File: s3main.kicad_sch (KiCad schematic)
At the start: 137 parts, among them J1 TRACK, J2 IDC, J3 POWER, J4 USB_C_Receptacle_USB2.0_16P, J5 ZUSI, Q1 QS6K21, Q10 BC847B, Q11 BC847B, Q2 BC847BDW1, Q3 SiS4634LDN, Q4 SiS4634LDN, Q5 SiS4634LDN, Q6 QS6K21, Q7 SiS4634LDN, Q8 SiS4634LDN, Q9 BC857B, SW1 EN, SW2 BOOT, U1 LM393, U10 BTS4141N, U2 7402, U3 TLV9061xDBV, U4 ESP32-S3-WROOM-2, U5 DRV8328B, U6 TPS281C100A, U7 AP63205WU, U8 TXS0102DCT, U9 AZ1117-3.3

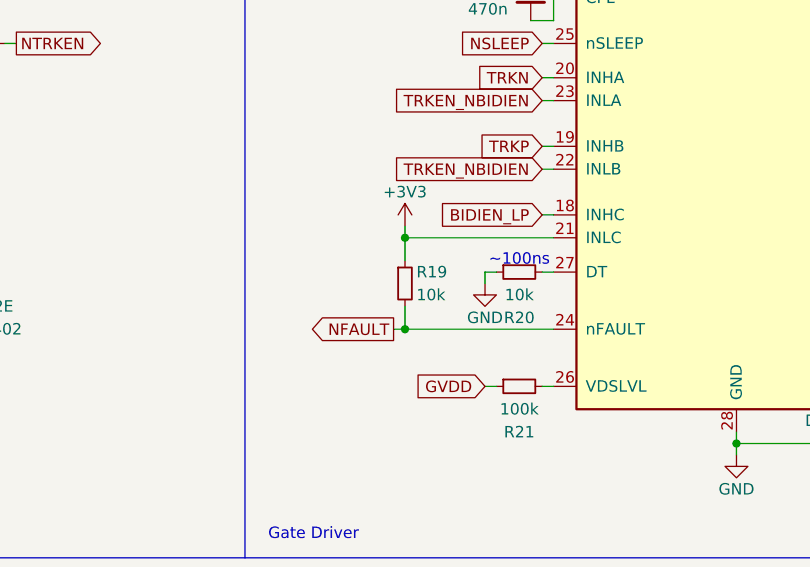
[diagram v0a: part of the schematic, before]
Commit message: chore: DNP R19
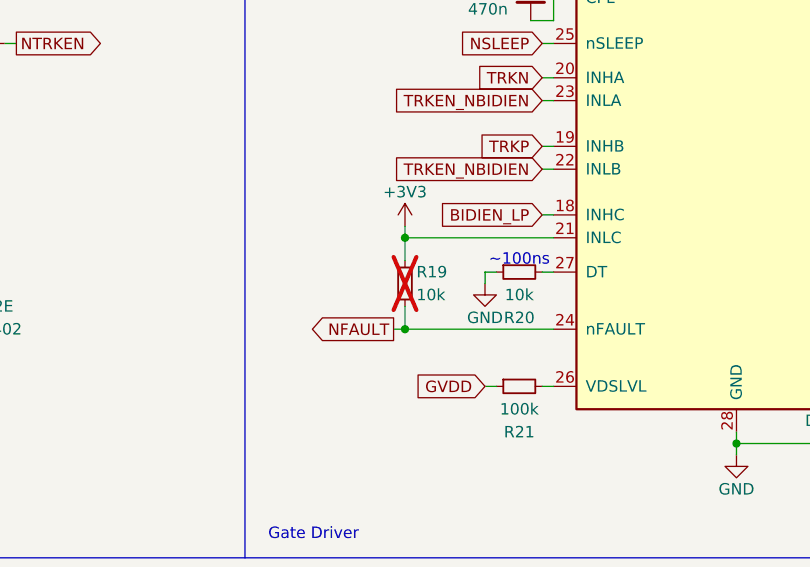
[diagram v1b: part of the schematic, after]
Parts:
- R19: now not fitted
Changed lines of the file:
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@@
 		(in_bom yes)
 		(on_board yes)
-		(dnp no)
+		(dnp yes)
 		(property "Reference" "R19"
 			(at 143.51 251.46 0)

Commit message: feat: new ACK circuit
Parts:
- removed Q10: BC847B, Package_TO_SOT_SMD:SOT-23, symbol Transistor_BJT:BC847
- removed Q9: BC857B, Package_TO_SOT_SMD:SOT-23-3, symbol Transistor_BJT:BC857
- removed R50, R52: 4k7, Resistor_SMD:R_0402_1005Metric, symbol Device:R_Small
- added C31: 10n, Capacitor_SMD:C_1206_3216Metric, symbol Device:C_Small
- added D14, D15: B5819W, Diode_SMD:D_SOD-123, symbol Device:D_Schottky_Small
- added D18: SBR3U60P1, Diode_SMD:D_PowerDI-123, symbol Device:D_Small
- added Q9: BSS138, Package_TO_SOT_SMD:TSOT-23, symbol Device:Q_NMOS_GSD
- added R54: 10k, Resistor_SMD:R_0402_1005Metric, symbol Device:R_Small
- R49: value 1k -> 4k7
- R51: value 22k -> 1k
- renumbered C31 to C32, C32 to C33, C33 to C34, C34 to C35, C35 to C36, C36 to C37, D14 to D16, D15 to D17, D17 to D19, Q11 to Q10, R55 to R50, R53 to R52, R54 to R53, R56 to R55
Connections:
- net +3V3: now also R54.1; no longer R50.1
- net +5V: now also R50.1, D14.1 (K)
- net ACK: now also Q9.3 (D), R54.2; no longer R50.2
- net GND: now also D15.2 (A), Q9.2 (S)
- net VDC: no longer R49.1
- net Vdrive: now also R49.1
- net at R51.1: now also R50.2, C31.2, D14.2 (A), D15.1 (K)
- net at R51.2: now also Q9.1 (G)
- net at J5.4 (Pin_4): now also D18.1 (K); no longer U10.1 (OUT)
- net at R49.2: now also C31.1
- new net: D18.2 (A), U10.1 (OUT)
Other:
- moved on the sheet: R50, U10

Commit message: build: update to KiCad 9.0.0
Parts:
- Q1, Q6: symbol Device:Q_Dual_NMOS_G1S2G2D2S1D1 -> Transistor_FET:Q_Dual_NMOS_G1S2G2D2S1D1
- Q9: symbol Device:Q_NMOS_GSD -> Transistor_FET:Q_NMOS_GSD

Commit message: feat: replace IO2 with VDRIVE_SEN
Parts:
- added R47: 14k3, Resistor_SMD:R_0402_1005Metric, symbol Device:R_Small
- added R48: 470, Resistor_SMD:R_0402_1005Metric, symbol Device:R_Small
- Q2: footprint Package_TO_SOT_SMD:SOT-363_SC-70-6 -> OpenRemise:SOT-363_SC-70-6
- renumbered C32 to C31, C31 to C32, Q9 to Q10, Q10 to Q9, R47 to R49, R48 to R50, R49 to R51, R50 to R54, R51 to R55, R55 to R56, R54 to R57
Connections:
- net GND: now also R48.2
- net NFAULT: now also J2.38 (Pin_38)
- net Vdrive: now also R47.1
- net IO1 renamed VDRIVE_SEN
- net VDRIVE_SEN: now also R47.2, R48.1; no longer J2.38 (Pin_38)
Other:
- moved on the sheet: C32, D14, D15, Q10, R51, R54, R55, R57

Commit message: chore: use consistent SOT-23-3 footprint
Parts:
- Q10: footprint Package_TO_SOT_SMD:TSOT-23 -> Package_TO_SOT_SMD:SOT-23
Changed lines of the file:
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@@
 			)
 		)
-		(property "Footprint" "Package_TO_SOT_SMD:TSOT-23"
+		(property "Footprint" "Package_TO_SOT_SMD:SOT-23"
 			(at 384.81 223.52 0)
 			(hide yes)
